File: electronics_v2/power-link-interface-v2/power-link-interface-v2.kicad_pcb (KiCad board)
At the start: 2 copper layers, 45 x 74 mm, 47 parts, among them J1 Conn_01x02, J2 Conn_01x03, J3 Conn_02x05_Odd_Even, J4 Conn_01x03, J5 Conn_01x03, J6 Conn_01x03, J7 Conn_01x03, Q1 IRFR5305, SW1 SW_Push_SPDT, U1 ESC, U2 MP1584, U3 LM258

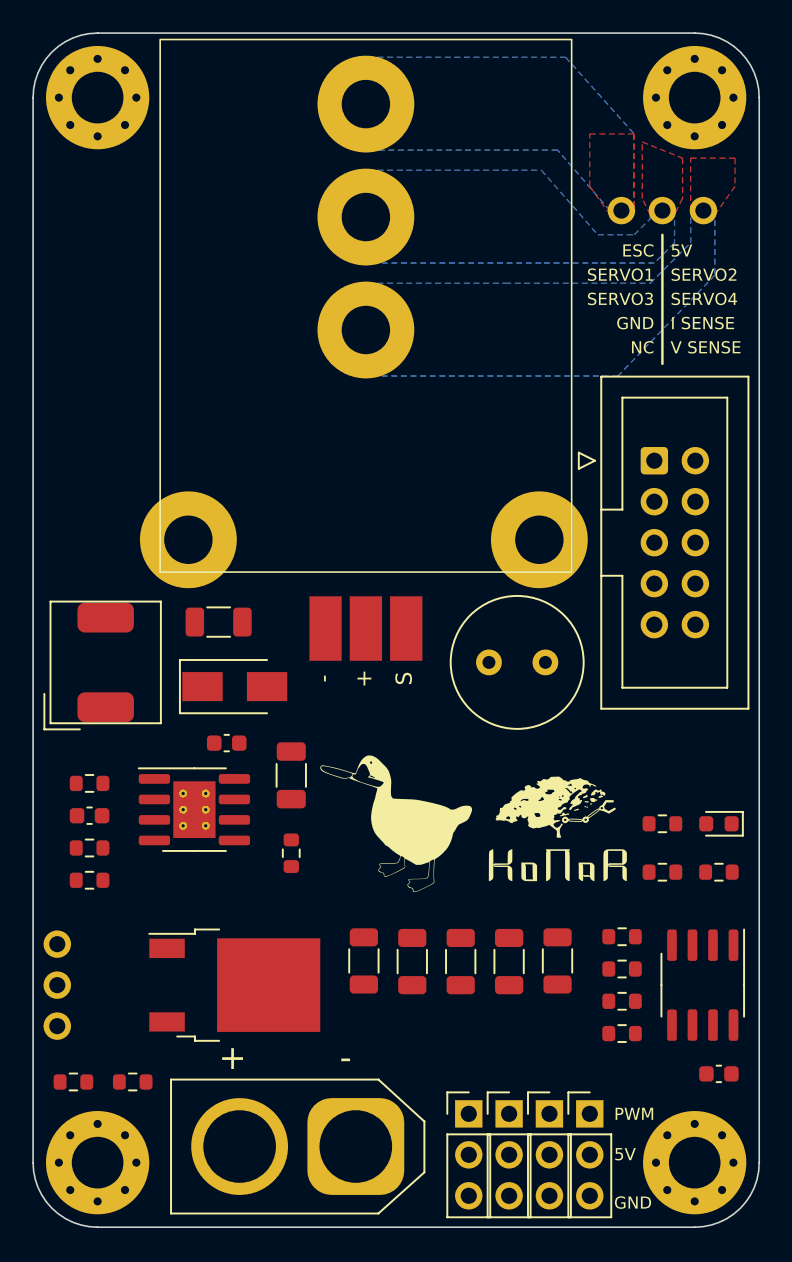
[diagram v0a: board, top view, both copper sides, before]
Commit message: edge XT60 connector & INA226 I2C measurement
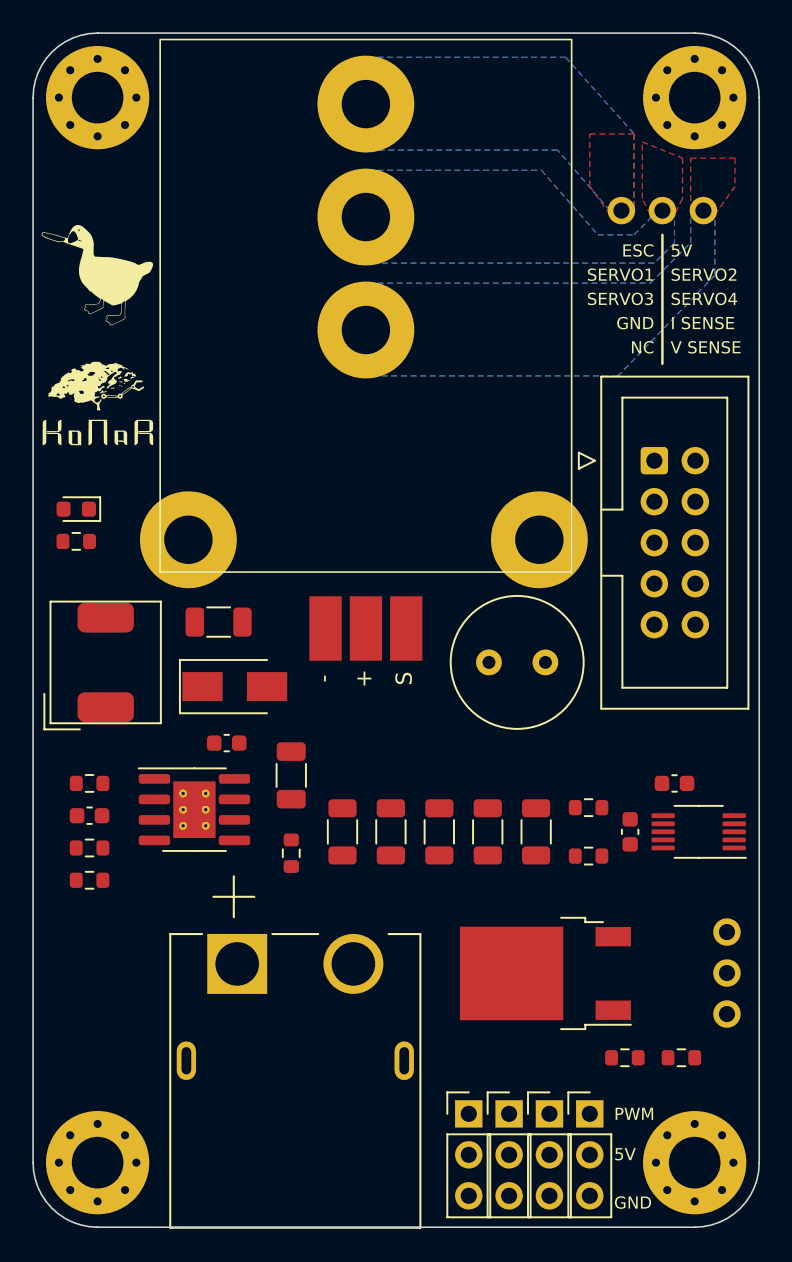
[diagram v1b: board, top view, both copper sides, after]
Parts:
- removed the G*** at (118.3, 94.0)
- removed the G*** at (130.0, 95.0)
- removed the G*** at (111.5, 88.0)
- removed R15, R16: 10k, Resistor_SMD:R_0603_1608Metric
- removed R17, R18: 470k, Resistor_SMD:R_0603_1608Metric
- removed the R3 at (136.5, 97.0)
- removed the R4 at (140.0, 97.0)
- added C6: 100n, Capacitor_SMD:C_0603_1608Metric, F.Cu at (134.5, 94.5)
- added G***: LOGO, LOGO, F.Cu at (100.2, 60.0)
- added G***: LOGO, LOGO, F.Cu at (101.5, 68.5)
- added G***: LOGO, LOGO, B.Cu at (111.8, 86.5)
- added R11: 10, Resistor_SMD:R_0603_1608Metric, F.Cu at (131.9, 96.0)
- added R12: 10, Resistor_SMD:R_0603_1608Metric, F.Cu at (131.9, 93.0)
- J1: footprint Connector_AMASS:AMASS_XT60-M_1x02_P7.20mm_Vertical -> goose:AMASS_XT60PW-M
- U3: value LM258 -> INA226; footprint Package_SO:SOIC-8_3.9x4.9mm_P1.27mm -> Package_SO:VSSOP-10_3x3mm_P0.5mm
- moved D1 44.3 mm to (100.2, 74.5)
- moved SW1 41.5 mm to (140.5, 105.8)
- moved R6 40.3 mm to (100.2, 76.5), turned to 180 degrees
- moved R2 37.7 mm to (137.7, 108.5), turned to 0 degrees
- moved R1 30.5 mm to (134.2, 108.5)
- moved Q1 19.3 mm to (129.2, 103.3), turned to 180 degrees
- moved C7 18.2 mm to (137.2, 91.5), turned to 180 degrees
- moved U3 9.50 mm to (138.8, 94.5), turned to 180 degrees
- moved R4 8.15 mm to (122.7, 94.5)
- moved R5 8.15 mm to (125.7, 94.5)
- moved R8 8.15 mm to (119.7, 94.5)
- moved R10 8.11 mm to (116.7, 94.5)
- moved R7 8.11 mm to (128.7, 94.5)
- moved J1 6.51 mm to (113.8, 108.7)
- renumbered C6 to C7, R12 to R10, R5 to R3, R7 to R4, R8 to R5, R9 to R7, R11 to R8, R10 to R9
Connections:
- net +BATT renamed VBUS
- C7 pad 2: /SUPPLY -> +5V
- J3 pad 10: /BATT_V_SENSE -> /I2C_SCL
- J3 pad 8: /BATT_I_SENSE -> /I2C_SDA
- U3 pad 1: /BATT_I_SENSE -> GND
- U3 pad 2: /COMP- -> GND
- U3 pad 3: /COMP+ -> unconnected-(U3-Pad3)
- U3 pad 4: GND -> /I2C_SDA
- U3 pad 5: (no net) -> /I2C_SCL
- U3 pad 6: (no net) -> +5V
- U3 pad 7: (no net) -> GND
- U3 pad 8: /SUPPLY -> /VIN-
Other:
- board text removed: "+"
- board text removed: "-"

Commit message: move XT60 to center of the edge
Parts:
- SW1: footprint goose:tht_pin_01x03 -> Button_Switch_THT:SW_CuK_JS202011CQN_DPDT_Straight
- moved D1 41.3 mm to (108.2, 115.0), turned to 0 degrees
- moved R6 37.4 mm to (108.2, 113.0), turned to 0 degrees
- moved J7 24.9 mm to (107.3, 109.0), turned to -90 degrees
- moved J6 22.9 mm to (107.3, 106.5), turned to -90 degrees
- moved J5 21.3 mm to (107.3, 104.0), turned to -90 degrees
- moved J4 20.2 mm to (107.3, 101.5), turned to -90 degrees
- moved SW1 6.46 mm to (140.9, 99.3), turned to -90 degrees
- moved J1 6.25 mm to (120.0, 108.8)
- moved R1 4.67 mm to (138.5, 110.2), turned to 0 degrees
- moved Q1 3.47 mm to (132.5, 104.5), turned to 90 degrees
- moved G*** 2.33 mm to (127.2, 102.8)
- moved R2 0.86 mm to (138.5, 108.2)
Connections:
- J1 pad 1: GND -> /BATTERY_IN
- J1 pad 2: /BATTERY_IN -> GND
